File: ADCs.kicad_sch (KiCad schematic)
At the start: 27 parts

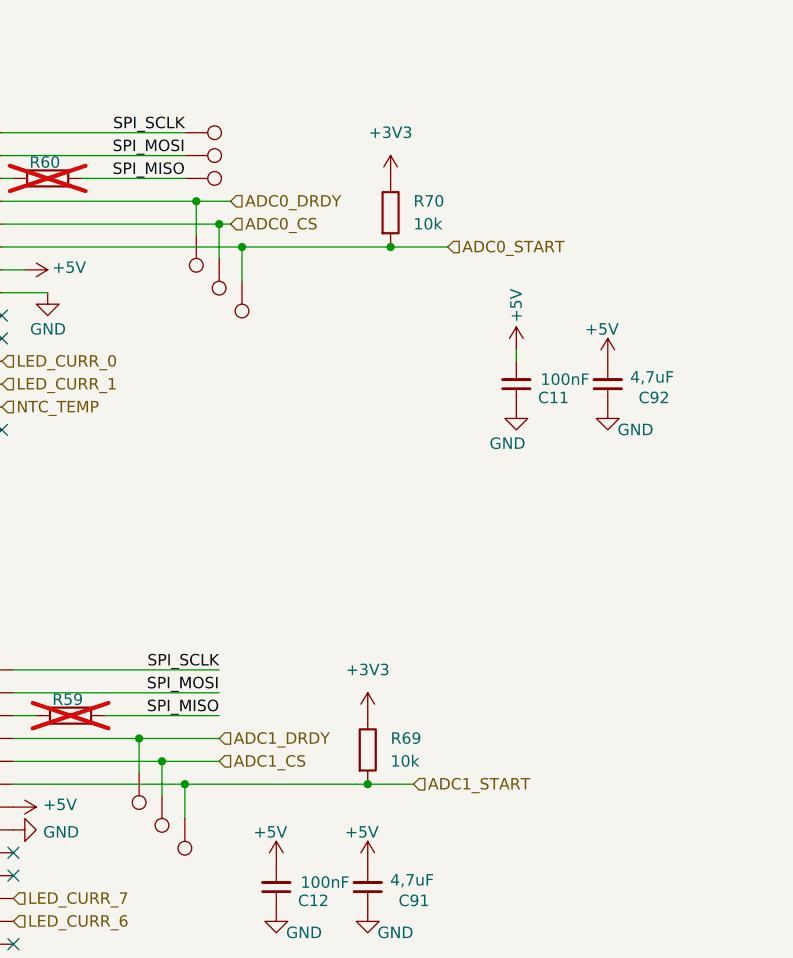
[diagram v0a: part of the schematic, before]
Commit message: Added low pass filters at current sense amp outputs and pull ups on cs pins, DRC done
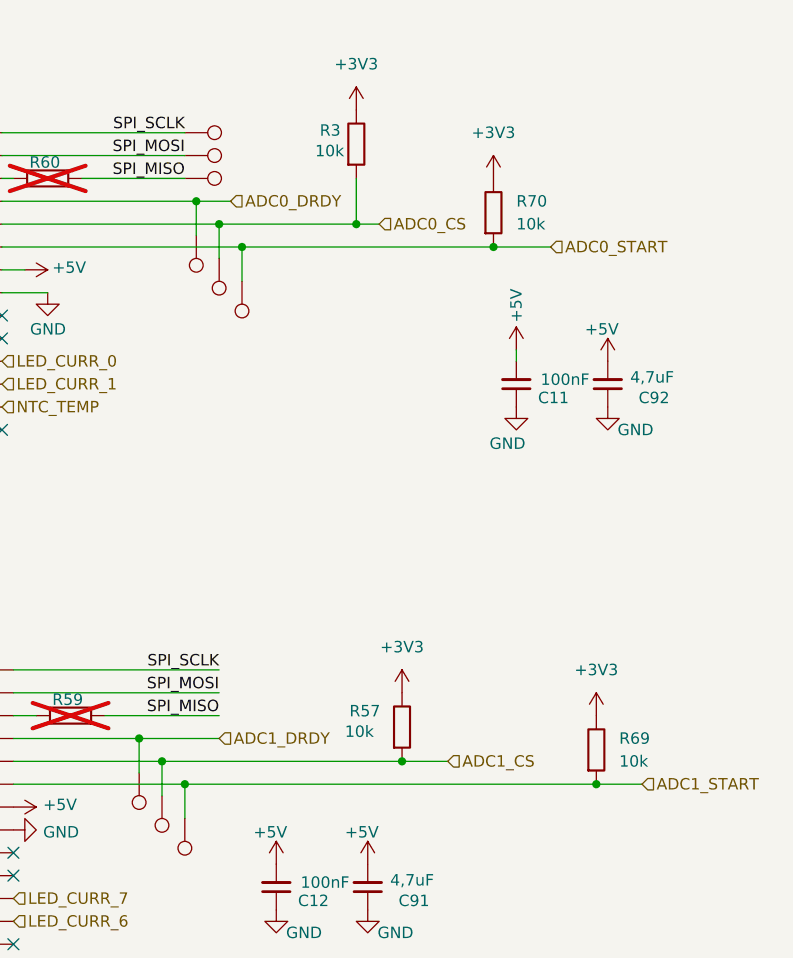
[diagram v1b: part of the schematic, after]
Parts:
- added R3, R57: 10k, Resistor_SMD:R_0603_1608Metric_Pad0.98x0.95mm_HandSolder, symbol PCM_SL_Resistors:Resistor
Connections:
- net +3V3: now also R3.2, R57.2
- net ADC0_CS: now also R3.1
- net ADC1_CS: now also R57.1
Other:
- moved on the sheet: R69, R70
